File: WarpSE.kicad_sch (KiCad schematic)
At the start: 9 parts

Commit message: Toward final "A"
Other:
- removed sheet DIPSW
- added sheet ClkBuf (ClkBuf.kicad_sch)
- sheet Buf ports: added GA[23..22]; removed none
- sheet Clk.sch ports: added FCLK, MCKE; removed CK20EN, CK25EN, RCLK
- sheet Control ports: added GA[23..22], MCKE; removed CK20EN, CK25EN, SW0, SW1, SW2

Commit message: RC
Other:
- sheet Control ports: added ROM~{OE}; removed ROM~{CS}
- sheet RAMROM ports: added ROM~{OE}; removed ROM~{CS}
- company: (none) -> Garrett's Workshop
- title: (none) -> WarpSE (GW4410A)
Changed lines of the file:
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@@
 (kicad_sch (version 20230121) (generator eeschema)
   (paper "A4")
+  (title_block
+    (title "WarpSE (GW4410A)")
+    (date "2024-03-27")
+    (rev "1.0")
+    (company "Garrett's Workshop")
+  )
   (junction (at 73.66 71.12) (diameter 0) (color 0 0 0 0)
   )
@@
       (effects (font (size 1.27 1.27)) (justify right))
     )
-    (pin "ROM~{CS}" output (at 106.68 106.68 0)
+    (pin "ROM~{OE}" output (at 106.68 106.68 0)
       (effects (font (size 1.27 1.27)) (justify right))
     )
@@
       (effects (font (size 1.27 1.27)) (justify left))
     )
-    (pin "ROM~{CS}" input (at 114.3 106.68 180)
-      (effects (font (size 1.27 1.27)) (justify left))
-    )
+    (pin "ROM~{OE}" input (at 114.3 106.68 180)
+      (effects (font (size 1.27 1.27)) (justify left))
+    )

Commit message: USB power
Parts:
- H1, H2, H3, H4, H5: value (none) -> ~

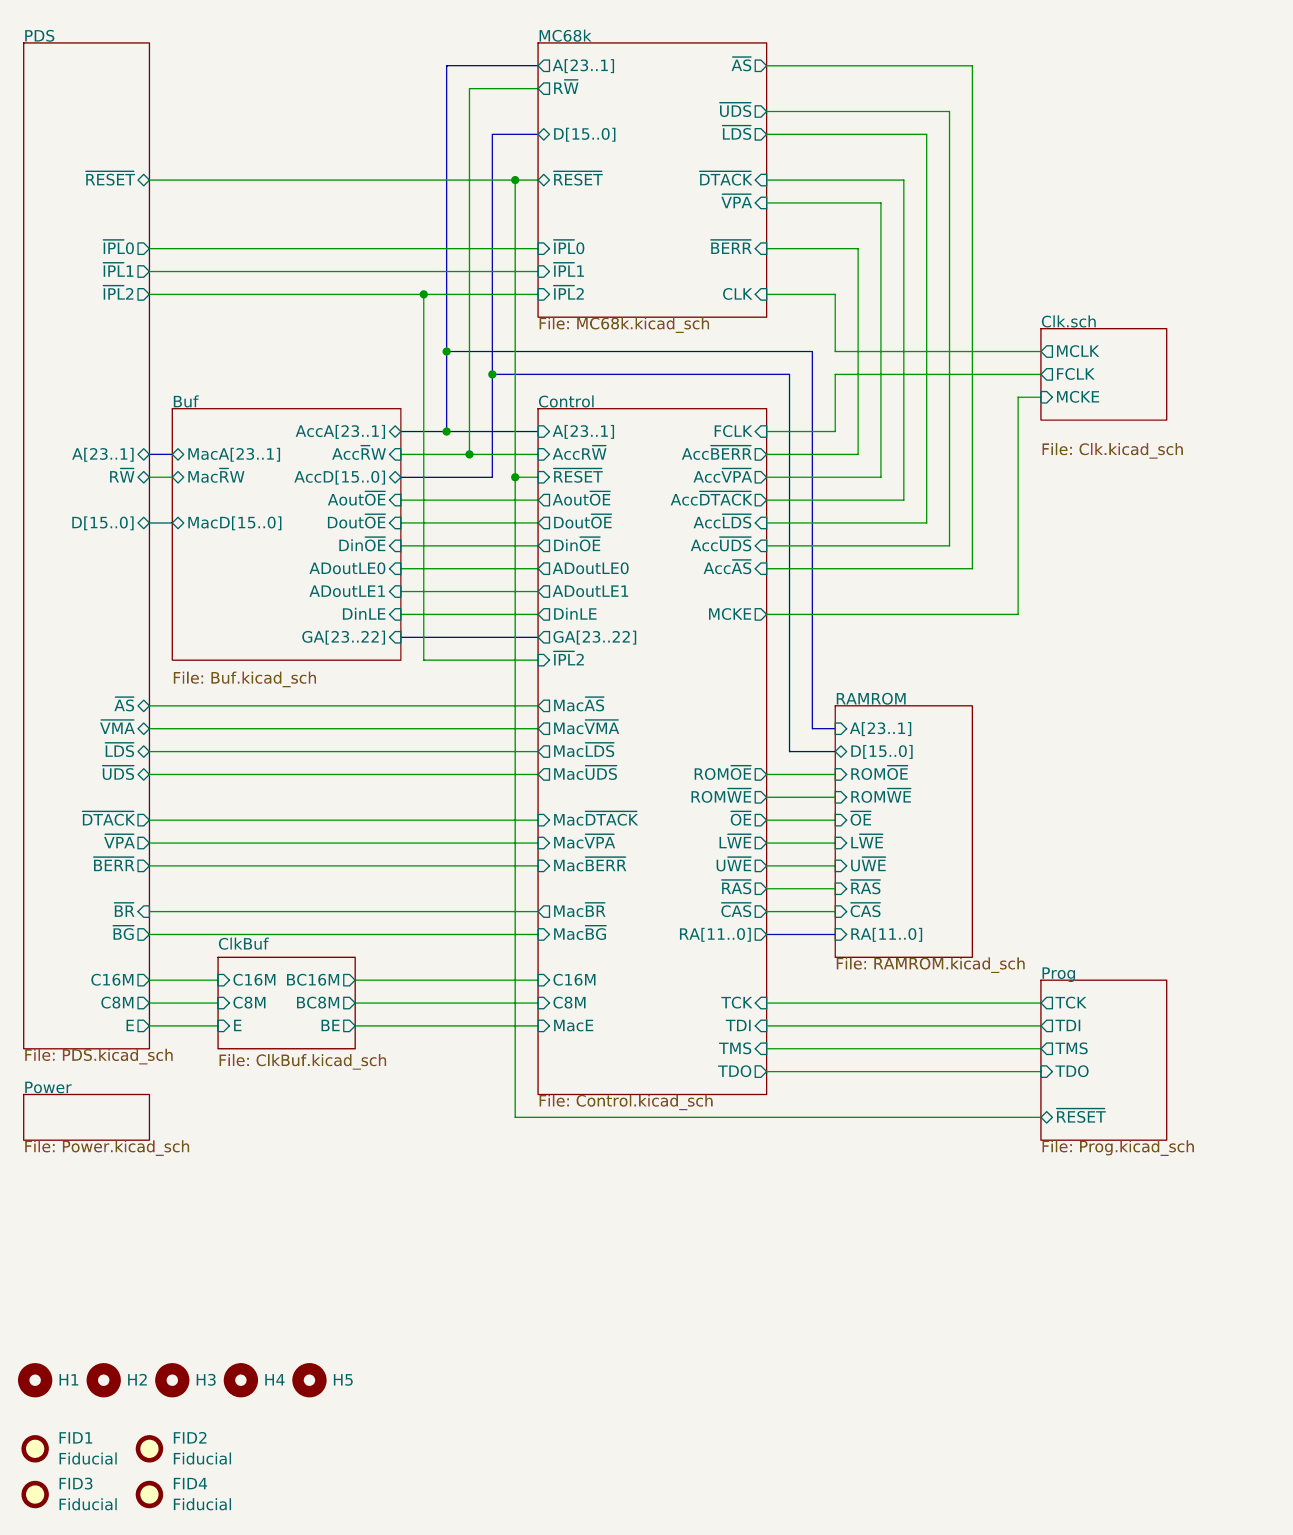
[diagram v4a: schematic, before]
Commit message: Board prerelease revision 3 with USB power, A[23:20] remapping
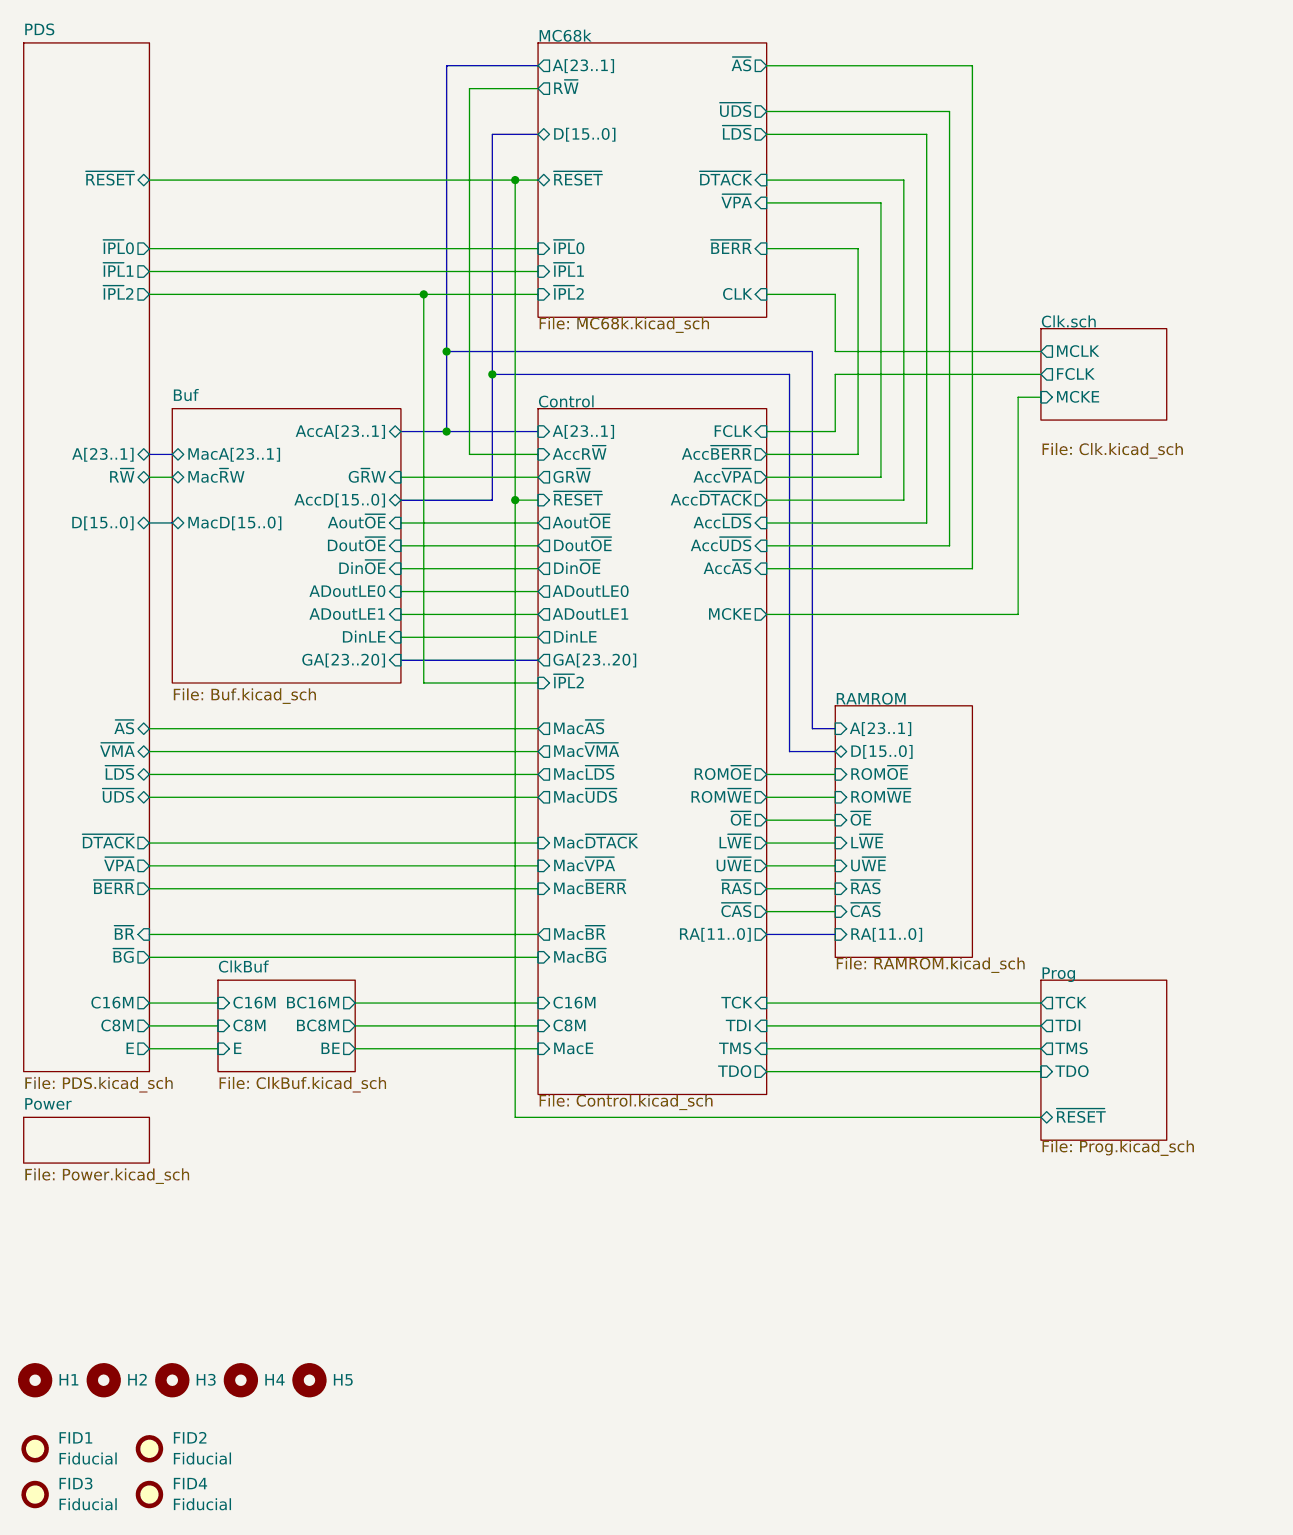
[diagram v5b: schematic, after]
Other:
- sheet Buf ports: added GA[23..20], G~{R}W; removed Acc~{R}W, GA[23..22]
- sheet Control ports: added GA[23..20], GR~{W}; removed GA[23..22]
